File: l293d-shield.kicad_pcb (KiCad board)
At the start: 2 copper layers, 53.3 x 43.2 mm, 3 parts, among them J1 Screw_Terminal_1x04, U1 l293d

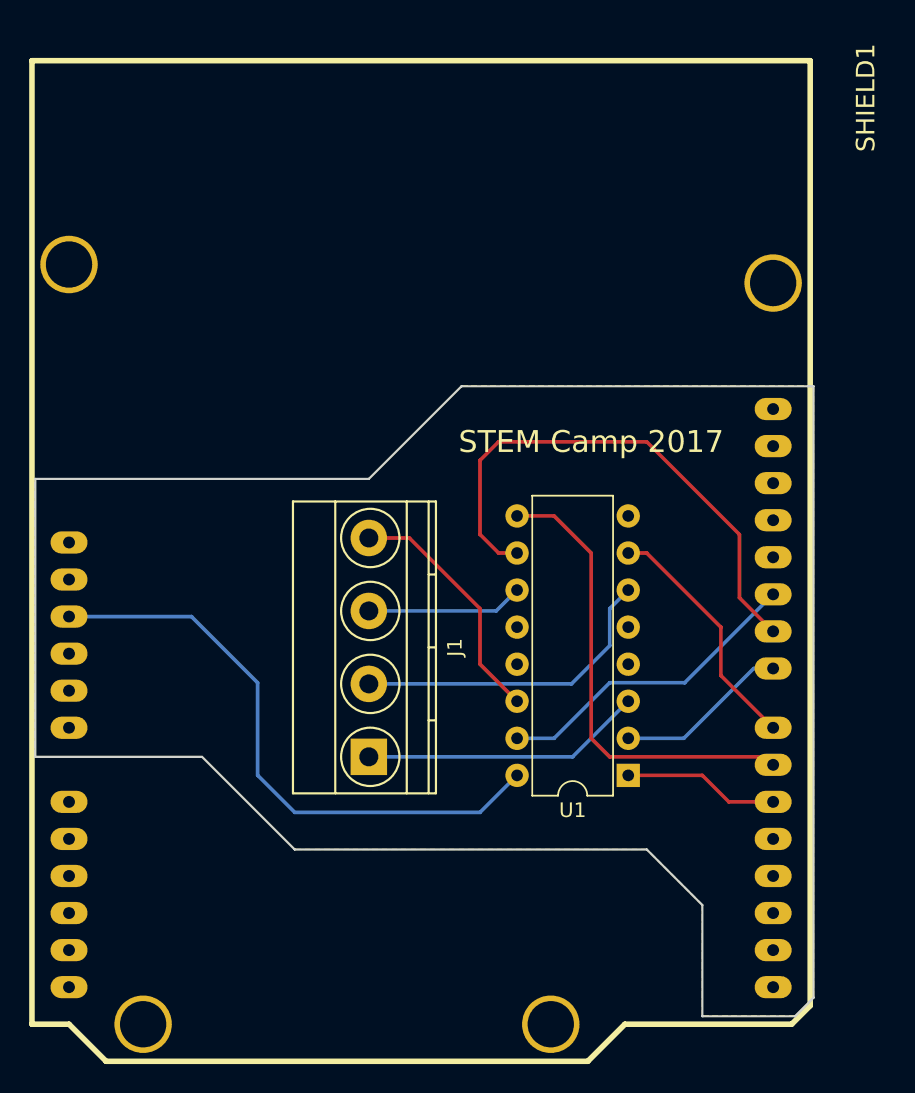
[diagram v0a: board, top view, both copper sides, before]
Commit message: Add battery connector and footprints
Add battery connector 1x2 .01" footprint
Add motor connector 1x4 .01" footprint
Fix global power nets in schematic
Add battery connector to shield
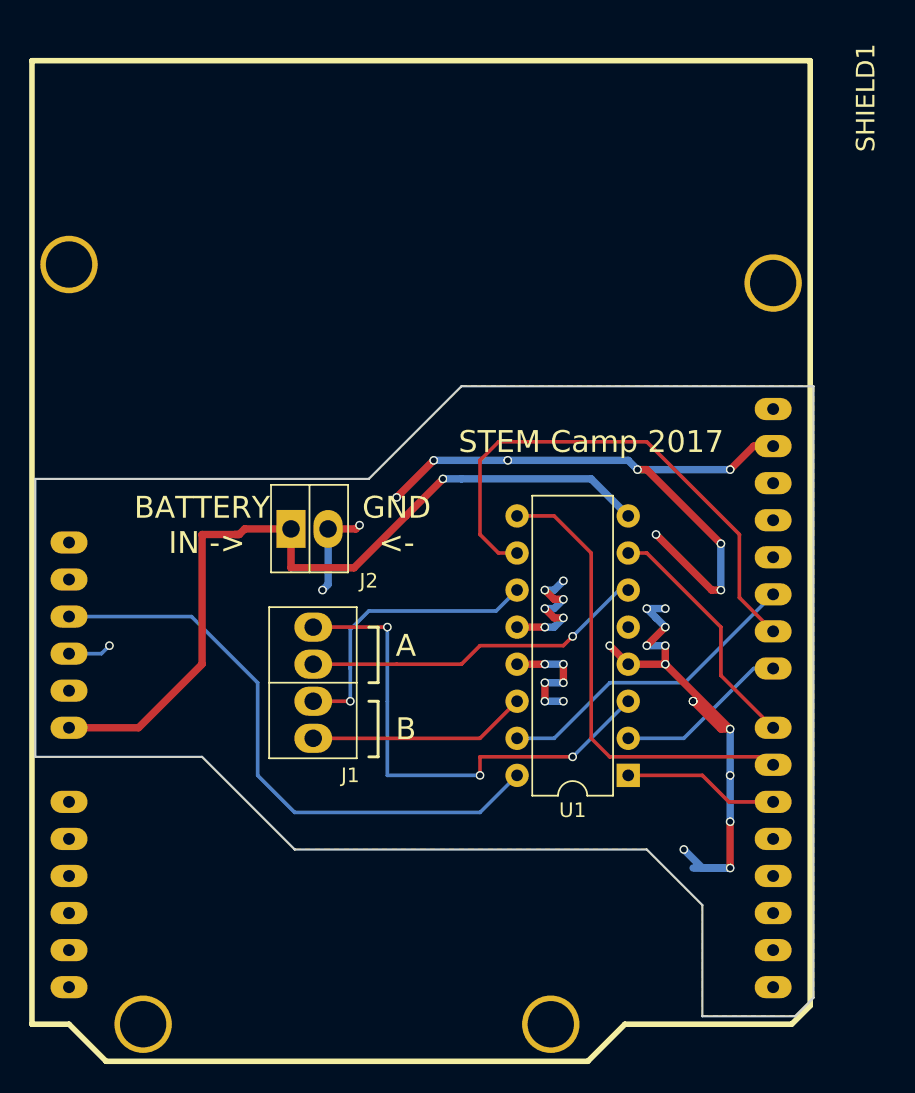
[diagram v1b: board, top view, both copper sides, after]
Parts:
- added J2: CONN_01X02, l293d-shield:Molex_KK-6410-02_02x2.54mm_Straight, F.Cu at (172.5, 86.0)
- J1: value Screw_Terminal_1x04 -> CONN_01X04; footprint Connectors_Terminal_Blocks:TerminalBlock_Pheonix_MKDS1.5-4pol -> l293d-shield:Molex_KK-6410-04_04x2.54mm_Straight
- moved J1 4.02 mm to (174.0, 100.3)
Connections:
- net Net-(SHIELD1-Pad10) renamed /IN4
- net Net-(SHIELD1-Pad5) renamed /1,2EN
- net Net-(SHIELD1-Pad5V) renamed +5V
- net Net-(SHIELD1-Pad6) renamed /3,4EN
- net Net-(SHIELD1-Pad7) renamed /IN2
- net Net-(SHIELD1-Pad8) renamed /IN1
- net Net-(SHIELD1-Pad9) renamed /IN3
- net Net-(SHIELD1-PadV_IN) renamed VCC
- J1 pad 1: Net-(J1-Pad1) -> /OUT_4
- J1 pad 2: Net-(J1-Pad2) -> /OUT_3
- J1 pad 3: Net-(J1-Pad3) -> /OUT_2
- J1 pad 4: Net-(J1-Pad4) -> /OUT_1
- SHIELD1 pad GND1: Net-(SHIELD1-PadGND1) -> GND
- SHIELD1 pad GND2: Net-(SHIELD1-PadGND2) -> GND
- SHIELD1 pad GND3: Net-(SHIELD1-PadGND3) -> GND
- U1 pad 11: Net-(J1-Pad3) -> /OUT_3
- U1 pad 12: Net-(U1-Pad12) -> GND
- U1 pad 13: Net-(U1-Pad13) -> GND
- U1 pad 14: Net-(J1-Pad4) -> /OUT_4
- U1 pad 3: Net-(J1-Pad1) -> /OUT_1
- U1 pad 4: Net-(SHIELD1-PadGND3) -> GND
- U1 pad 5: Net-(U1-Pad5) -> GND
- U1 pad 6: Net-(J1-Pad2) -> /OUT_2
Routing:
- net GND: track 0.00 -> 113.0 mm, vias 0 -> 37
- net VCC: track 0.00 -> 56.2 mm, vias 0 -> 1
- net /OUT_1: track 0.00 -> 34.9 mm, vias 0 -> 3
- net /OUT_2: track 0.00 -> 23.7 mm, vias 0 -> 1
- net Net-(J1-Pad2): track 21.9 -> 0.00 mm
- net /OUT_3: track 0.00 -> 20.6 mm, vias 0 -> 1
- net Net-(J1-Pad1): track 19.4 -> 0.00 mm
- net Net-(J1-Pad4): track 17.0 -> 0.00 mm
- net /OUT_4: track 0.00 -> 15.0 mm
- net Net-(J1-Pad3): track 10.8 -> 0.00 mm
- added copper zone on B.Cu, net GND
- added copper zone on F.Cu, net GND
- removed copper zone on F.Cu, net Net-(SHIELD1-PadGND3)
- removed copper zone on B.Cu, net VCC
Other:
- net class Power added: clearance 0.2, trace_width 0.508, via_dia 0.6, via_drill 0.4
- board text added: "A"
- board text added: "B"
- board text added: "BATTERY IN ->"
- board text added: "GND <-"

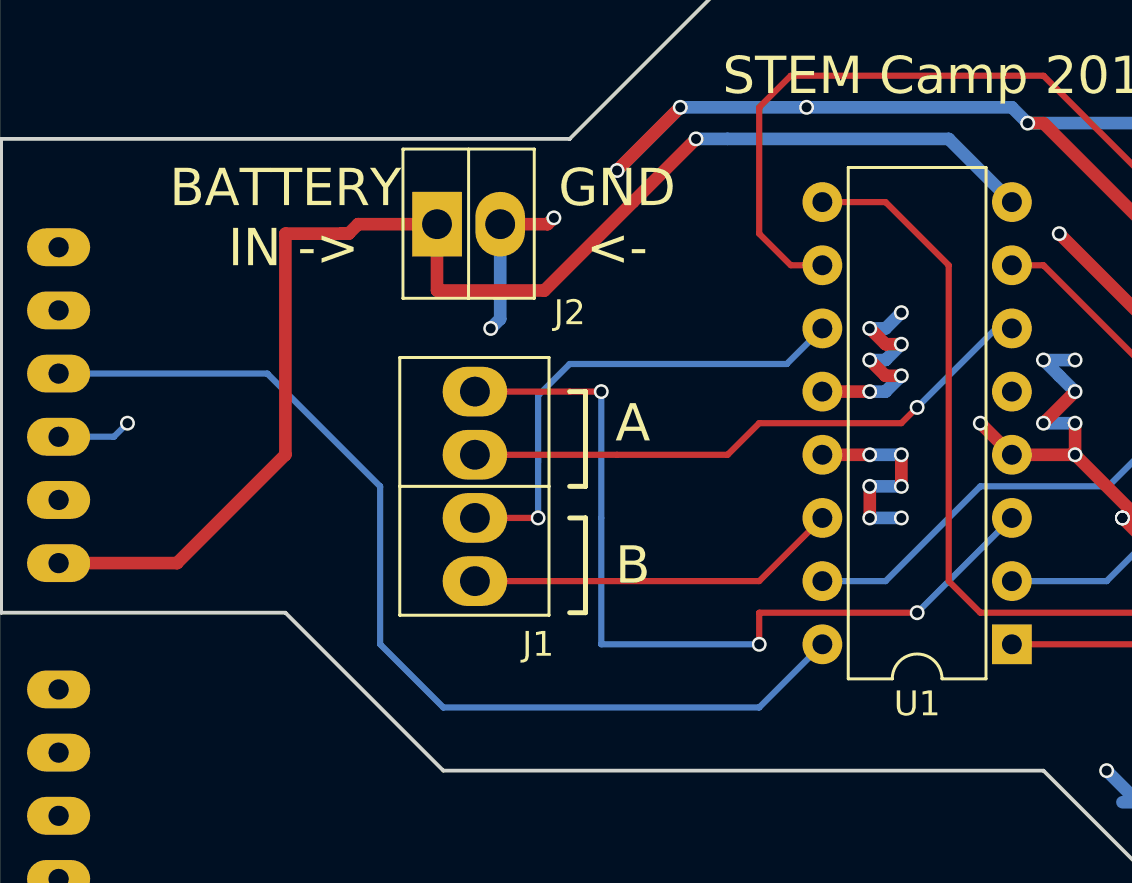
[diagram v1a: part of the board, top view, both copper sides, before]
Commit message: Improve PCB layout and markings
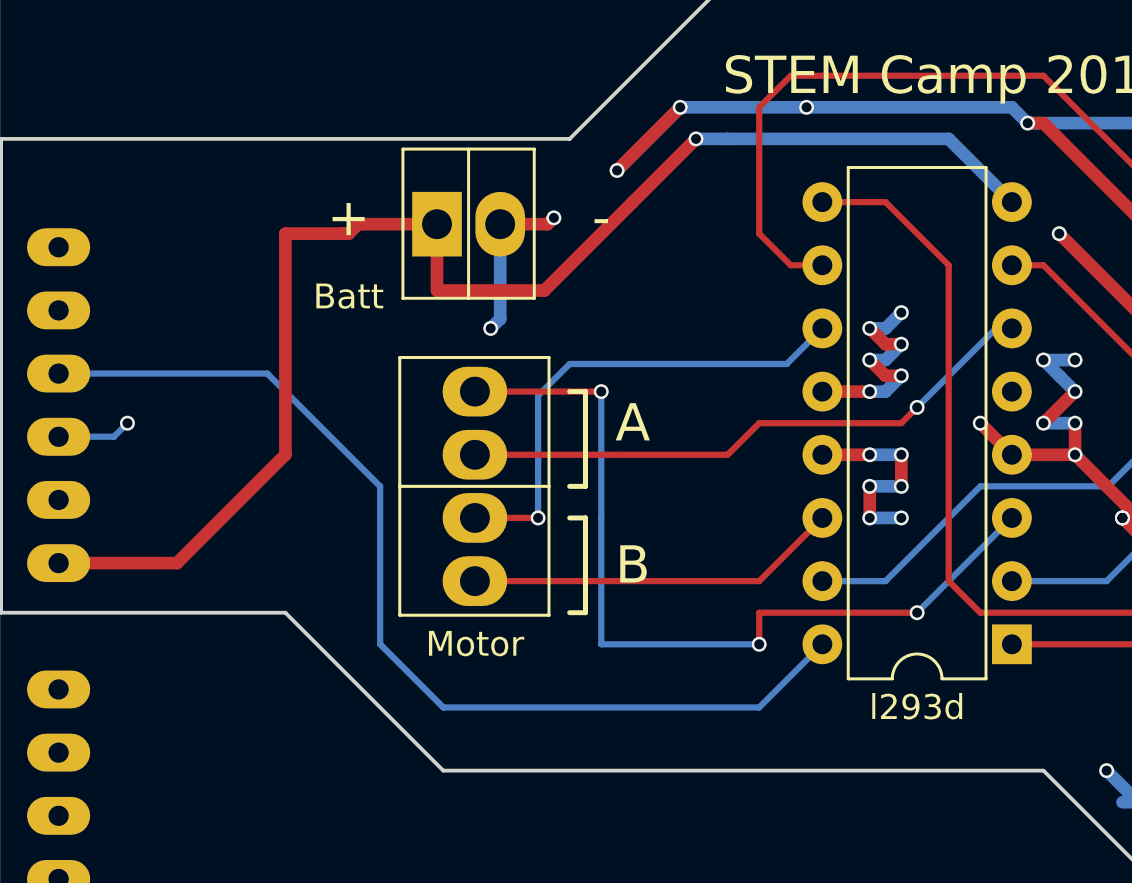
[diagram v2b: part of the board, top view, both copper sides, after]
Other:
- board text added: "+"
- board text added: "-"
- board text added: "Batt"
- board text added: "Motor"
- board text added: "l293d"
- board text removed: "BATTERY IN ->"
- board text removed: "GND <-"
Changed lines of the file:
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@@
     (area 154.2614 49.295529 213.433 122.856601)
     (thickness 1.6)
-    (drawings 23)
+    (drawings 26)
     (tracks 171)
     (zones 0)
@@
     (descr "16-lead dip package, row spacing 7.62 mm (300 mils)")
     (tags "DIL DIP PDIP 2.54mm 7.62mm 300mil")
-    (fp_text reference U1 (at 3.81 -2.39 180) (layer F.SilkS)
+    (fp_text reference U1 (at 3.81 -2.39 180) (layer F.SilkS) hide
       (effects (font (size 1 1) (thickness 0.15)))
     )
@@
     (descr "Connector Headers with Friction Lock, 22-27-2041, http://www.molex.com/pdm_docs/sd/022272021_sd.pdf")
     (tags "connector molex kk_6410 22-27-2041")
-    (fp_text reference J1 (at -2.54 2.54 180) (layer F.SilkS)
+    (fp_text reference J1 (at -2.54 2.54 180) (layer F.SilkS) hide
       (effects (font (size 1 1) (thickness 0.15)))
     )
@@
     (descr "Connector Headers with Friction Lock, 22-27-2021, http://www.molex.com/pdm_docs/sd/022272021_sd.pdf")
     (tags "connector molex kk_6410 22-27-2021")
-    (fp_text reference J2 (at 5.334 3.556) (layer F.SilkS)
+    (fp_text reference J2 (at 5.334 3.556) (layer F.SilkS) hide
       (effects (font (size 1 1) (thickness 0.15)))
     )
@@
       (net 29 GND))
   )
-  (gr_text "GND\n<-" (at 179.705 85.725) (layer F.SilkS)
-    (effects (font (size 1.5 1.5) (thickness 0.3)))
+  (gr_text Motor (at 173.99 102.87) (layer F.SilkS)
+    (effects (font (size 1 1) (thickness 0.15)))
+  )
+  (gr_text Batt (at 168.91 88.9) (layer F.SilkS)
+    (effects (font (size 1 1) (thickness 0.15)))
+  )
+  (gr_text l293d (at 191.77 105.41) (layer F.SilkS)
+    (effects (font (size 1 1) (thickness 0.15)))
+  )
+  (gr_text - (at 179.07 85.725) (layer F.SilkS)
+    (effects (font (size 1.5 1.5) (thickness 0.375)))
   )
   (gr_line (start 178.435 92.71) (end 177.8 92.71) (layer F.SilkS) (width 0.2))
@@
     (effects (font (size 1.5 1.5) (thickness 0.3)))
   )
-  (gr_text "BATTERY\n IN ->" (at 166.37 85.725) (layer F.SilkS)
-    (effects (font (size 1.5 1.5) (thickness 0.3)))
+  (gr_text + (at 168.91 85.725) (layer F.SilkS)
+    (effects (font (size 1.5 1.5) (thickness 0.375)))
   )
   (gr_text "STEM Camp 2017" (at 193.04 80.01) (layer F.SilkS)

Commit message: Improve power handling
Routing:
- net GND: track 113.0 -> 152.5 mm, vias 37 -> 45
- net /OUT_1: track 34.9 -> 40.0 mm
- net +5V: track 41.0 -> 38.1 mm
- net /OUT_4: track 15.0 -> 16.8 mm
- net (no net): track 0.00 -> 1.27 mm

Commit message: fix stray trace
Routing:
- net GND: track 152.5 -> 221.7 mm
- net /OUT_4: track 16.8 -> 15.0 mm
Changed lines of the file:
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@@
   (general
     (links 20)
-    (no_connects 1)
+    (no_connects 0)
     (area 154.2614 49.295529 213.433 122.856601)
     (thickness 1.6)
     (drawings 26)
-    (tracks 193)
+    (tracks 211)
     (zones 0)
     (modules 4)
@@
   )
   (setup
-    (last_trace_width 0.508)
+    (last_trace_width 0.25)
     (user_trace_width 0.508)
     (trace_clearance 0.2)
@@
     (visible_elements FFFFFF7F)
     (pcbplotparams
-      (layerselection 0x00030_80000001)
-      (usegerberextensions false)
+      (layerselection 0x010f0_80000001)
+      (usegerberextensions true)
       (excludeedgelayer true)
       (linewidth 0.100000)
@@
       (plotinvisibletext false)
       (padsonsilk false)
-      (subtractmaskfromsilk false)
+      (subtractmaskfromsilk true)
       (outputformat 1)
       (mirror false)
-      (drillshape 1)
+      (drillshape 0)
       (scaleselection 1)
-      (outputdirectory ""))
+      (outputdirectory out/))
   )
   (net 0 "")
@@
   (segment (start 192.405 93.345) (end 191.77 93.345) (width 0.508) (layer B.Cu) (net 19))
   (segment (start 195.58 90.17) (end 192.405 93.345) (width 0.508) (layer B.Cu) (net 19))
-  (segment (start 173.99 100.33) (end 175.26 99.06) (width 0.508) (layer F.Cu) (net 20))
   (segment (start 187.96 97.79) (end 185.42 100.33) (width 0.508) (layer F.Cu) (net 20))
   (segment (start 173.99 100.33) (end 175.798 100.33) (width 0.508) (layer F.Cu) (net 20))
@@
   (segment (start 160.5661 91.9861) (end 170.18 101.6) (width 0.508) (layer B.Cu) (net 28))
   (segment (start 157.2514 91.9861) (end 160.5661 91.9861) (width 0.508) (layer B.Cu) (net 28))
+  (segment (start 191.135 96.52) (end 192.58999 95.06501) (width 0.25) (layer F.Cu) (net 29))
+  (segment (start 193.49001 89.995954) (end 204.553146 101.05909) (width 0.25) (layer F.Cu) (net 29))
+  (segment (start 204.553146 101.05909) (end 206.469654 101.05909) (width 0.25) (layer F.Cu) (net 29))
+  (segment (start 187.419999 83.964999) (end 190.011409 83.964999) (width 0.25) (layer F.Cu) (net 29))
+  (segment (start 192.58999 95.06501) (end 192.58999 90.30499) (width 0.25) (layer F.Cu) (net 29))
+  (segment (start 192.58999 90.30499) (end 188.500001 86.215001) (width 0.25) (layer F.Cu) (net 29))
+  (segment (start 188.500001 86.215001) (end 187.419999 86.215001) (width 0.25) (layer F.Cu) (net 29))
+  (segment (start 186.834999 85.630001) (end 186.834999 84.549999) (width 0.25) (layer F.Cu) (net 29))
+  (segment (start 187.419999 86.215001) (end 186.834999 85.630001) (width 0.25) (layer F.Cu) (net 29))
+  (segment (start 186.834999 84.549999) (end 187.419999 83.964999) (width 0.25) (layer F.Cu) (net 29))
+  (segment (start 190.011409 83.964999) (end 193.49001 87.4436) (width 0.25) (layer F.Cu) (net 29))
+  (segment (start 193.49001 87.4436) (end 193.49001 89.995954) (width 0.25) (layer F.Cu) (net 29))
+  (segment (start 206.469654 101.05909) (end 207.10641 101.695846) (width 0.25) (layer F.Cu) (net 29))
+  (segment (start 207.10641 101.695846) (end 207.10641 105.136354) (width 0.25) (layer F.Cu) (net 29))
+  (segment (start 207.10641 105.136354) (end 206.469654 105.77311) (width 0.25) (layer F.Cu) (net 29))
+  (segment (start 194.1236 102.05001) (end 190.5 98.42641) (width 0.25) (layer F.Cu) (net 29))
+  (segment (start 206.469654 105.77311) (end 196.298108 105.77311) (width 0.25) (layer F.Cu) (net 29))
+  (segment (start 196.298108 105.77311) (end 194.1236 103.598602) (width 0.25) (layer F.Cu) (net 29))
+  (segment (start 194.1236 103.598602) (end 194.1236 102.05001) (width 0.25) (layer F.Cu) (net 29))
   (segment (start 181.61 86.36) (end 181.61 85.09) (width 0.508) (layer B.Cu) (net 29))
   (segment (start 181.61 85.09) (end 182.11799 85.59799) (width 0.508) (layer B.Cu) (net 29))

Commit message: fix
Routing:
- net GND: track 221.7 -> 152.5 mm
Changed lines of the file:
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@@
     (thickness 1.6)
     (drawings 26)
-    (tracks 211)
+    (tracks 192)
     (zones 0)
     (modules 4)
@@
   (segment (start 160.5661 91.9861) (end 170.18 101.6) (width 0.508) (layer B.Cu) (net 28))
   (segment (start 157.2514 91.9861) (end 160.5661 91.9861) (width 0.508) (layer B.Cu) (net 28))
-  (segment (start 191.135 96.52) (end 192.58999 95.06501) (width 0.25) (layer F.Cu) (net 29))
-  (segment (start 193.49001 89.995954) (end 204.553146 101.05909) (width 0.25) (layer F.Cu) (net 29))
-  (segment (start 204.553146 101.05909) (end 206.469654 101.05909) (width 0.25) (layer F.Cu) (net 29))
-  (segment (start 187.419999 83.964999) (end 190.011409 83.964999) (width 0.25) (layer F.Cu) (net 29))
-  (segment (start 192.58999 95.06501) (end 192.58999 90.30499) (width 0.25) (layer F.Cu) (net 29))
-  (segment (start 192.58999 90.30499) (end 188.500001 86.215001) (width 0.25) (layer F.Cu) (net 29))
-  (segment (start 188.500001 86.215001) (end 187.419999 86.215001) (width 0.25) (layer F.Cu) (net 29))
-  (segment (start 186.834999 85.630001) (end 186.834999 84.549999) (width 0.25) (layer F.Cu) (net 29))
-  (segment (start 187.419999 86.215001) (end 186.834999 85.630001) (width 0.25) (layer F.Cu) (net 29))
-  (segment (start 186.834999 84.549999) (end 187.419999 83.964999) (width 0.25) (layer F.Cu) (net 29))
-  (segment (start 190.011409 83.964999) (end 193.49001 87.4436) (width 0.25) (layer F.Cu) (net 29))
-  (segment (start 193.49001 87.4436) (end 193.49001 89.995954) (width 0.25) (layer F.Cu) (net 29))
-  (segment (start 206.469654 101.05909) (end 207.10641 101.695846) (width 0.25) (layer F.Cu) (net 29))
-  (segment (start 207.10641 101.695846) (end 207.10641 105.136354) (width 0.25) (layer F.Cu) (net 29))
-  (segment (start 207.10641 105.136354) (end 206.469654 105.77311) (width 0.25) (layer F.Cu) (net 29))
-  (segment (start 194.1236 102.05001) (end 190.5 98.42641) (width 0.25) (layer F.Cu) (net 29))
-  (segment (start 206.469654 105.77311) (end 196.298108 105.77311) (width 0.25) (layer F.Cu) (net 29))
-  (segment (start 196.298108 105.77311) (end 194.1236 103.598602) (width 0.25) (layer F.Cu) (net 29))
-  (segment (start 194.1236 103.598602) (end 194.1236 102.05001) (width 0.25) (layer F.Cu) (net 29))
   (segment (start 181.61 86.36) (end 181.61 85.09) (width 0.508) (layer B.Cu) (net 29))
   (segment (start 181.61 85.09) (end 182.11799 85.59799) (width 0.508) (layer B.Cu) (net 29))

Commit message: Generaate output files
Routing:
- net (no net): track 1.27 -> 0.00 mm
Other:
- board text added: "L293D"
- board text removed: "l293d"
